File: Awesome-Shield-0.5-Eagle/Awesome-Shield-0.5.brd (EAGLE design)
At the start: 100 x 80 mm, 24 parts, among them J1 ARDUINO_R3_SHIELDUNO_R3_SHIEL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, SW1 SPST_TACT-EVQQ2

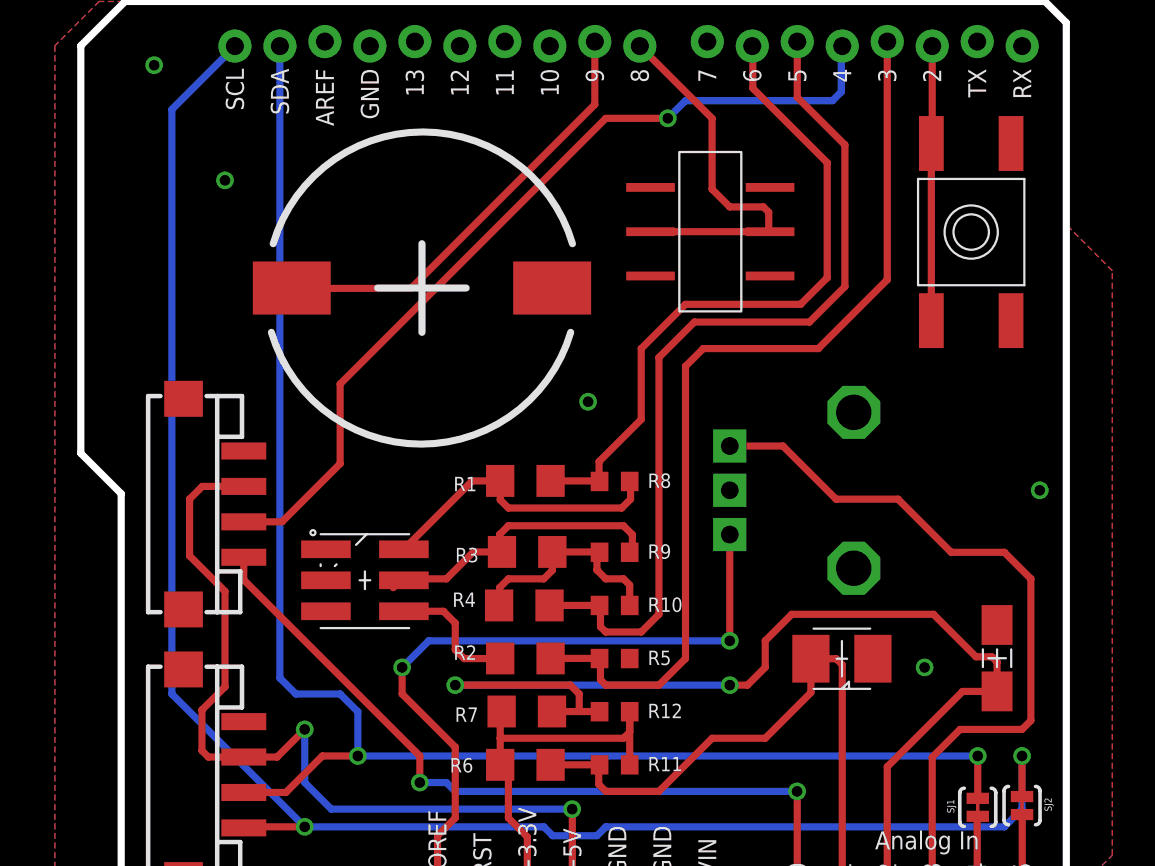
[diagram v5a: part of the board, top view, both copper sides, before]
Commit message: moved one grove port aka 4pin connector for UX
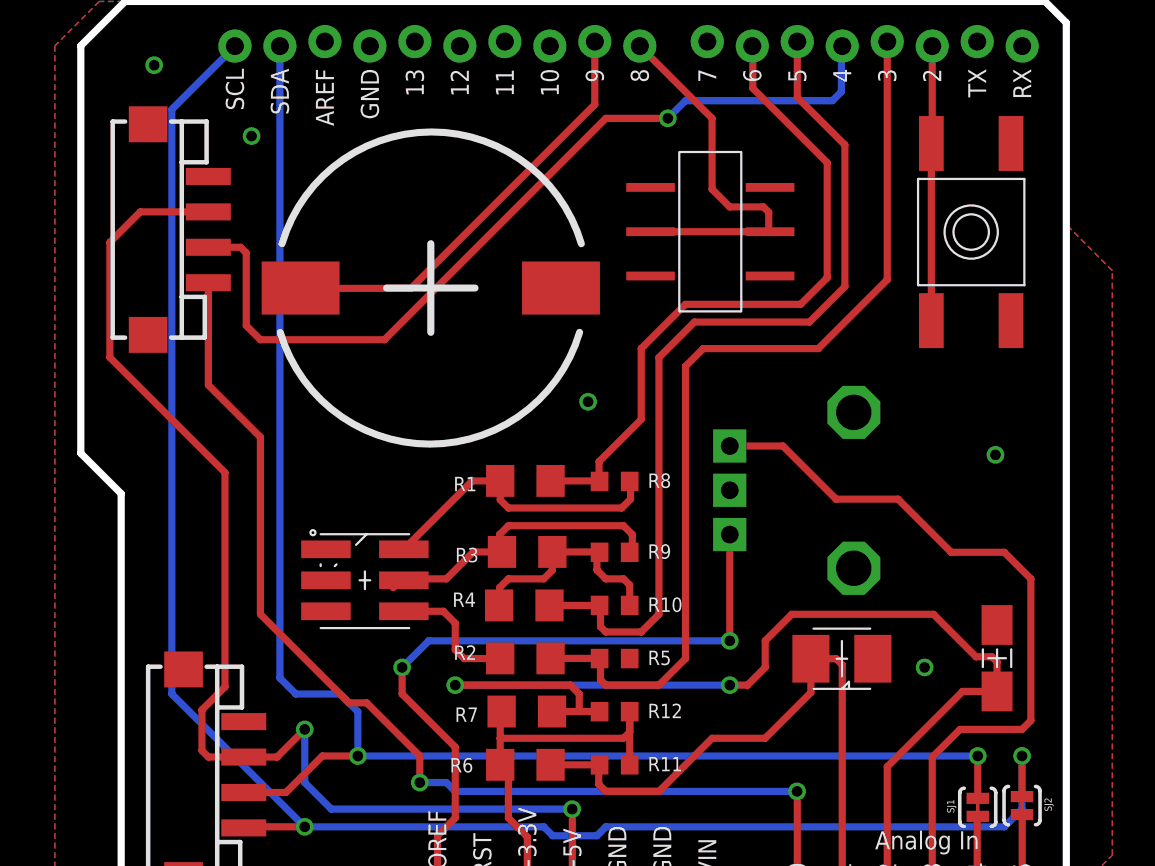
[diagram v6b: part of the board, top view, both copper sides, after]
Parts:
- moved J2 15.6 mm to (34.1, 58.2)
- moved SG1 0.50 mm to (46.6, 54.9)
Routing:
- net +5V: track 49.7 -> 69.0 mm
- net A0: track 44.8 -> 61.7 mm
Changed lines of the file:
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@@
 <attribute name="VALUE" x="32.885" y="25.535" size="0.8128" layer="27" font="vector" ratio="10" rot="R90"/>
 </element>
-<element name="J2" library="Connector " package="4P-SMD-2.0" value="" x="36.06" y="42.72" smashed="yes" rot="R90">
-<attribute name="VALUE" x="32.885" y="40.815" size="0.8128" layer="27" font="vector" ratio="10" rot="R90"/>
-</element>
-<element name="SG1" library="SparkFun-Electromechanical" package="BUZZER-CCV" value="BUZZERSMD2" x="46.12" y="54.92"/>
+<element name="J2" library="Connector " package="4P-SMD-2.0" value="" x="34.06" y="58.22" smashed="yes" rot="R90">
+<attribute name="VALUE" x="30.885" y="56.315" size="0.8128" layer="27" font="vector" ratio="10" rot="R90"/>
+</element>
+<element name="SG1" library="SparkFun-Electromechanical" package="BUZZER-CCV" value="BUZZERSMD2" x="46.62" y="54.92"/>
 <element name="SJ1" library="SparkFun-Passives" package="PAD-JUMPER-2-NC_BY_TRACE_YES_SILK" value="JUMPER-PAD-2-NC_BY_TRACE" x="77.5" y="25.6" smashed="yes" rot="R270">
 <attribute name="NAME" x="75.77" y="26.0525" size="0.4064" layer="25" rot="R270"/>
@@
 <vertex x="81.3" y="71.1"/>
 </polygon>
-<via x="35" y="61" extent="1-16" drill="0.6"/>
-<via x="81" y="43.5" extent="1-16" drill="0.6"/>
+<via x="36.5" y="63.5" extent="1-16" drill="0.6"/>
+<via x="78.5" y="45.5" extent="1-16" drill="0.6"/>
 <via x="40.5" y="21.5" extent="1-16" drill="0.6"/>
 <via x="55.5" y="48.5" extent="1-16" drill="0.6"/>
@@
 <via x="31" y="67.5" extent="1-16" drill="0.6"/>
 <wire x1="79.38" y1="63.08" x2="87.5" y2="73" width="0" layer="19" extent="1-1"/>
-<wire x1="91.5" y1="37" x2="81" y2="43.5" width="0" layer="19" extent="1-1"/>
+<wire x1="91.5" y1="37" x2="78.59" y2="35.895" width="0" layer="19" extent="1-1"/>
 </signal>
 <signal name="A2">
@@
 <via x="54.6" y="25.5" extent="1-16" drill="0.6"/>
 <wire x1="54.6" y1="25.5" x2="41" y2="25.5" width="0.4064" layer="16"/>
-<wire x1="36.06" y1="43.72" x2="33.72" y2="43.72" width="0.4064" layer="1"/>
-<wire x1="33.72" y1="43.72" x2="33" y2="43" width="0.4064" layer="1"/>
-<wire x1="33" y1="43" x2="33" y2="39.8" width="0.4064" layer="1"/>
-<wire x1="33" y1="39.8" x2="35" y2="37.8" width="0.4064" layer="1"/>
-<wire x1="35" y1="37.8" x2="35" y2="32.4" width="0.4064" layer="1"/>
 <wire x1="35" y1="32.4" x2="33.7" y2="31.1" width="0.4064" layer="1"/>
 <wire x1="33.7" y1="31.1" x2="33.7" y2="28.8" width="0.4064" layer="1"/>
@@
 <wire x1="39.5" y1="30" x2="37.94" y2="28.44" width="0.4064" layer="1"/>
 <wire x1="36.06" y1="28.44" x2="37.94" y2="28.44" width="0.4064" layer="1"/>
+<wire x1="35" y1="32.4" x2="35" y2="44.5" width="0.4064" layer="1"/>
+<wire x1="35" y1="44.5" x2="28.5" y2="51" width="0.4064" layer="1"/>
+<wire x1="28.5" y1="51" x2="28.5" y2="57.5" width="0.4064" layer="1"/>
+<wire x1="28.5" y1="57.5" x2="30.22" y2="59.22" width="0.4064" layer="1"/>
+<wire x1="34.06" y1="59.22" x2="30.22" y2="59.22" width="0.4064" layer="1"/>
 </signal>
 <signal name="A0">
@@
 <via x="46" y="27" extent="1-16" drill="0.6"/>
 <wire x1="46" y1="27" x2="46" y2="28.5" width="0.4064" layer="1"/>
-<wire x1="46" y1="28.5" x2="36.06" y2="38.44" width="0.4064" layer="1"/>
 <wire x1="46" y1="27" x2="47.5" y2="27" width="0.4064" layer="16"/>
 <wire x1="47.5" y1="27" x2="48" y2="26.5" width="0.4064" layer="16"/>
-<wire x1="36.06" y1="39.72" x2="36.06" y2="38.44" width="0.4064" layer="1"/>
+<wire x1="34.06" y1="55.22" x2="34.06" y2="49.44" width="0.4064" layer="1"/>
+<wire x1="34.06" y1="49.44" x2="37" y2="46.5" width="0.4064" layer="1"/>
+<wire x1="37" y1="46.5" x2="37" y2="36.5" width="0.4064" layer="1"/>
+<wire x1="37" y1="36.5" x2="42" y2="31.5" width="0.4064" layer="1"/>
+<wire x1="42" y1="31.5" x2="43" y2="31.5" width="0.4064" layer="1"/>
+<wire x1="43" y1="31.5" x2="46" y2="28.5" width="0.4064" layer="1"/>
 </signal>
 <signal name="A5">
@@
 <contactref element="SG1" pad="-"/>
 <wire x1="55.88" y1="68.834" x2="55.88" y2="65.28" width="0.4064" layer="1"/>
-<wire x1="45.5" y1="54.9" x2="38.79" y2="54.9" width="0.4064" layer="1"/>
-<wire x1="38.79" y1="54.9" x2="38.77" y2="54.92" width="0.4064" layer="1"/>
 <wire x1="55.88" y1="65.28" x2="45.5" y2="54.9" width="0.4064" layer="1"/>
+<wire x1="38.79" y1="54.9" x2="45.5" y2="54.9" width="0.4064" layer="1"/>
+<wire x1="38.79" y1="54.9" x2="39.27" y2="54.92" width="0" layer="19" extent="1-1"/>
 </signal>
 <signal name="D4">
@@
 <wire x1="69.8" y1="66" x2="69.8" y2="68.53" width="0.4064" layer="16"/>
 <wire x1="69.8" y1="68.53" x2="69.85" y2="68.58" width="0.4064" layer="16"/>
-<wire x1="41.5" y1="49.5" x2="41.5" y2="45" width="0.4064" layer="1"/>
 <wire x1="60" y1="64.5" x2="56.5" y2="64.5" width="0.4064" layer="1"/>
-<wire x1="56.5" y1="64.5" x2="41.5" y2="49.5" width="0.4064" layer="1"/>
-<wire x1="41.5" y1="45" x2="38.22" y2="41.72" width="0.4064" layer="1"/>
-<wire x1="36.06" y1="41.72" x2="38.22" y2="41.72" width="0.4064" layer="1"/>
+<wire x1="56.5" y1="64.5" x2="44" y2="52" width="0.4064" layer="1"/>
+<wire x1="44" y1="52" x2="37" y2="52" width="0.4064" layer="1"/>
+<wire x1="34.06" y1="57.22" x2="35.88" y2="57.22" width="0.4064" layer="1"/>
+<wire x1="35.88" y1="57.22" x2="36.2" y2="56.9" width="0.4064" layer="1"/>
+<wire x1="36.2" y1="56.9" x2="36.2" y2="52.8" width="0.4064" layer="1"/>
+<wire x1="36.2" y1="52.8" x2="37" y2="52" width="0.4064" layer="1"/>
 </signal>
 <signal name="N$2">

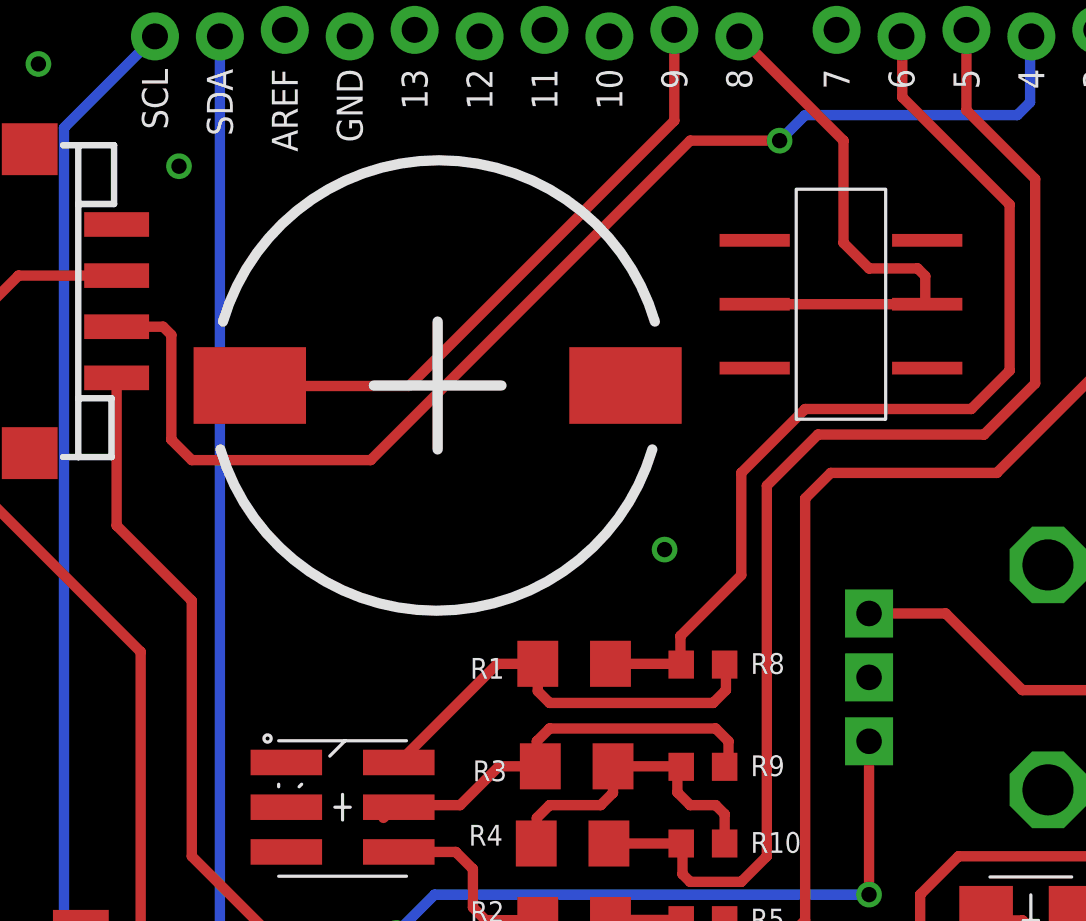
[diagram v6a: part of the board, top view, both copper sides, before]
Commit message: nudged traces for spacing
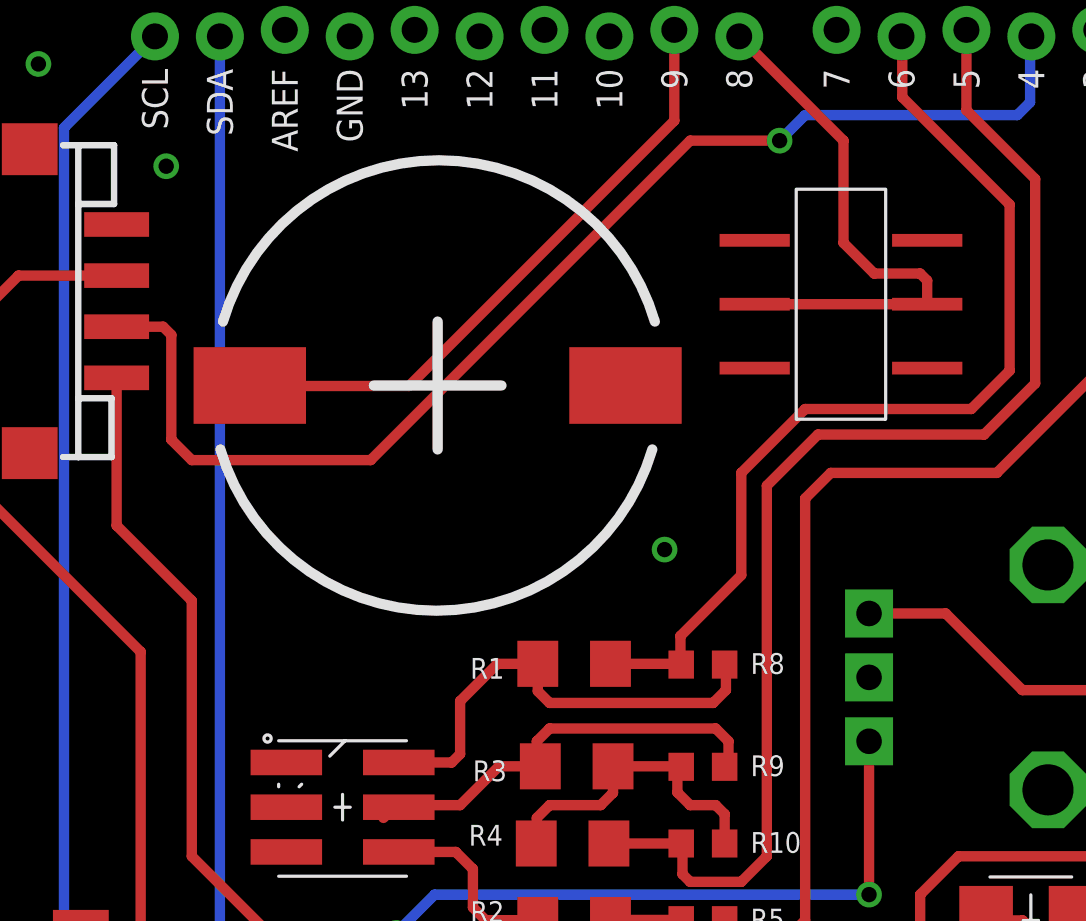
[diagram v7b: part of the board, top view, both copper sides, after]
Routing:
- net N$8: track 16.9 -> 18.1 mm
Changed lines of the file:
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@@
 <vertex x="81.3" y="71.1"/>
 </polygon>
-<via x="36.5" y="63.5" extent="1-16" drill="0.6"/>
+<via x="36" y="63.5" extent="1-16" drill="0.6"/>
 <via x="78.5" y="45.5" extent="1-16" drill="0.6"/>
 <via x="40.5" y="21.5" extent="1-16" drill="0.6"/>
@@
 <wire x1="58.42" y1="68.58" x2="62.5" y2="64.5" width="0.4064" layer="1"/>
 <wire x1="62.5" y1="64.5" x2="62.5" y2="60.5" width="0.4064" layer="1"/>
-<wire x1="62.5" y1="60.5" x2="63.5" y2="59.5" width="0.4064" layer="1"/>
-<wire x1="63.5" y1="59.5" x2="65.4" y2="59.5" width="0.4064" layer="1"/>
-<wire x1="65.4" y1="59.5" x2="65.7" y2="59.2" width="0.4064" layer="1"/>
-<wire x1="65.7" y1="59.2" x2="65.7" y2="58.175" width="0.4064" layer="1"/>
-<wire x1="65.7" y1="58.175" x2="65.775" y2="58.1" width="0.4064" layer="1"/>
+<wire x1="62.5" y1="60.5" x2="63.7" y2="59.3" width="0.4064" layer="1"/>
+<wire x1="65.775" y1="58.1" x2="65.775" y2="59.025" width="0.4064" layer="1"/>
+<wire x1="65.775" y1="59.025" x2="65.5" y2="59.3" width="0.4064" layer="1"/>
+<wire x1="65.5" y1="59.3" x2="63.7" y2="59.3" width="0.4064" layer="1"/>
 </signal>
 <signal name="D9">
@@
 <contactref element="R1" pad="2"/>
 <wire x1="50.538" y1="44.03" x2="48.96" y2="44.03" width="0.4064" layer="1"/>
-<wire x1="48.96" y1="44.03" x2="45.1" y2="40.17" width="0.4064" layer="1"/>
 <wire x1="50.538" y1="44.03" x2="50.538" y2="42.962" width="0.4064" layer="1"/>
 <wire x1="50.538" y1="42.962" x2="51" y2="42.5" width="0.4064" layer="1"/>
@@
 <wire x1="57.9" y1="43" x2="57.9" y2="43.95" width="0.4064" layer="1"/>
 <wire x1="57.9" y1="43.95" x2="57.85" y2="44" width="0.4064" layer="1"/>
+<wire x1="45.1" y1="40.17" x2="47.17" y2="40.17" width="0.4064" layer="1"/>
+<wire x1="47.17" y1="40.17" x2="47.5" y2="40.5" width="0.4064" layer="1"/>
+<wire x1="47.5" y1="40.5" x2="47.5" y2="42.57" width="0.4064" layer="1"/>
+<wire x1="47.5" y1="42.57" x2="48.96" y2="44.03" width="0.4064" layer="1"/>
 </signal>
 <signal name="D3">

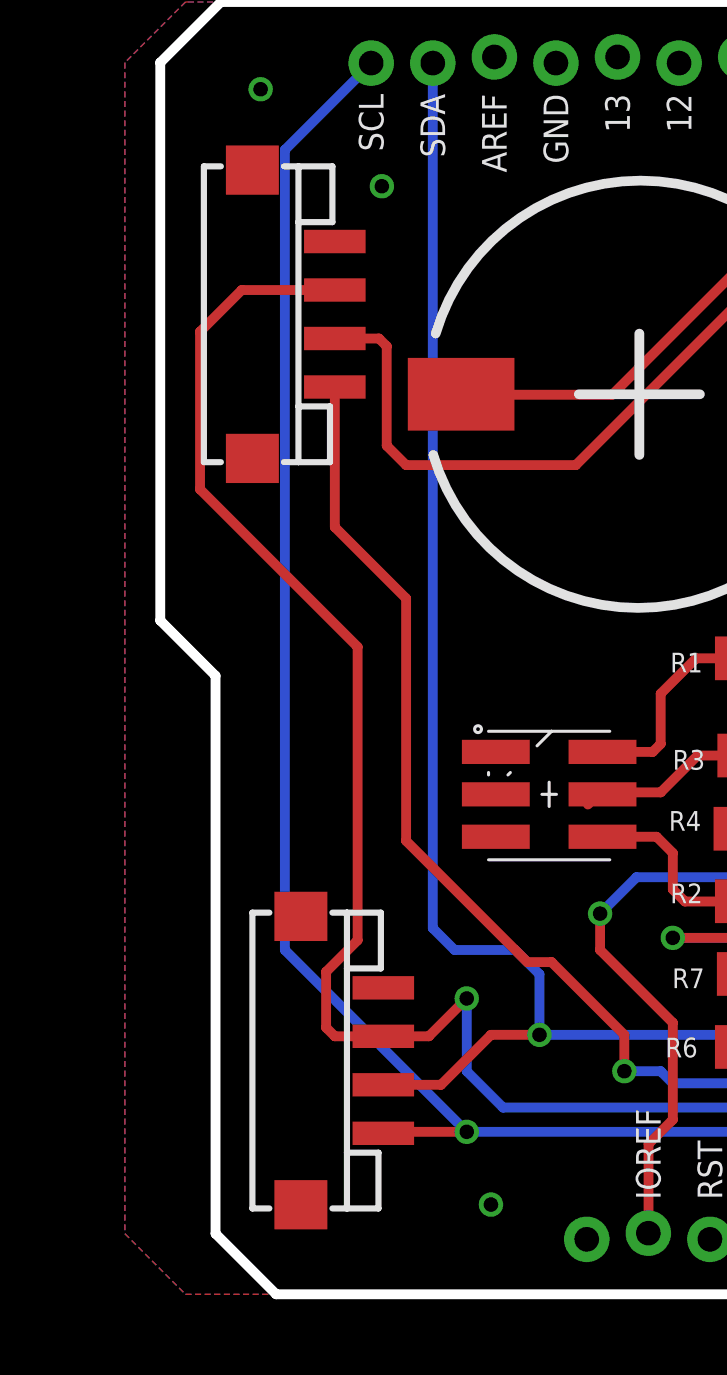
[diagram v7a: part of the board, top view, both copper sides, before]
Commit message: updated 4pin connectors to official seeed version
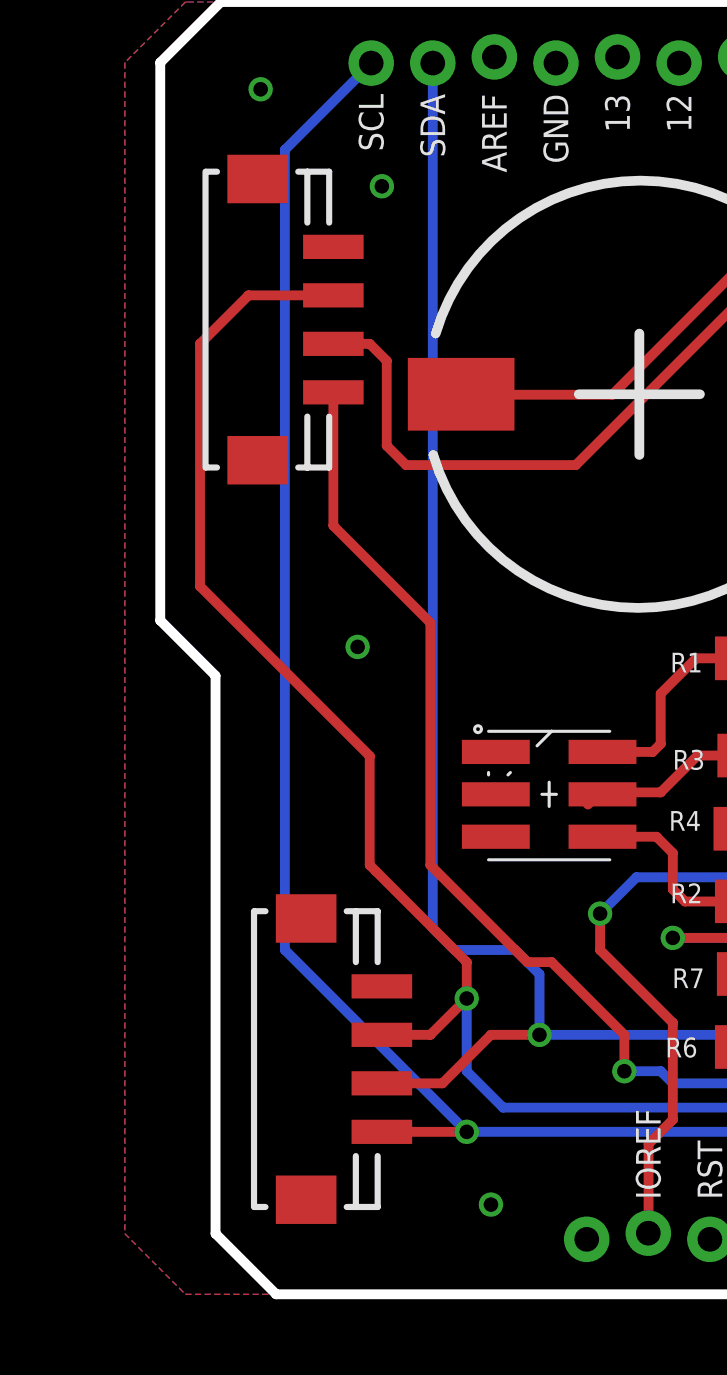
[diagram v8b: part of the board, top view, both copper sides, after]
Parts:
- removed J2, J5: (no value), Connector :4P-SMD-2.0
- added J3, J4: (no value), Seeed-OPL-Connector:HW4-SMD-2.0
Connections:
- net +5V: now also J3.3, J4.3; no longer J2.3, J5.3
- net A0: now also J4.1; no longer J2.1
- net D4: now also J4.2; no longer J2.2
- net GND: now also J3.4, J3.SS1, J3.SS2, J4.4, J4.SS1, J4.SS2; no longer J2.4, J2.SS1, J2.SS2, J5.4, J5.SS1, J5.SS2
- net SCL: now also J3.1; no longer J5.1
- net SDA: now also J3.2; no longer J5.2
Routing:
- net +5V: track 69.0 -> 66.2 mm
